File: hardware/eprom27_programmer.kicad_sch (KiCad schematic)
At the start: 37 parts, among them IC1 74595D, IC2 74595D, IC3 27512, J1 JACK-PLUG1, Q1 BC557, Q2 BC557, Q3 BC557, Q4 BC557, Q5 BC557, Q6 BC547, Q7 BC547, Q8 BC547, U1 NANO, U2 DC-DC-STEP-UP-MT3608, X1 MPT2

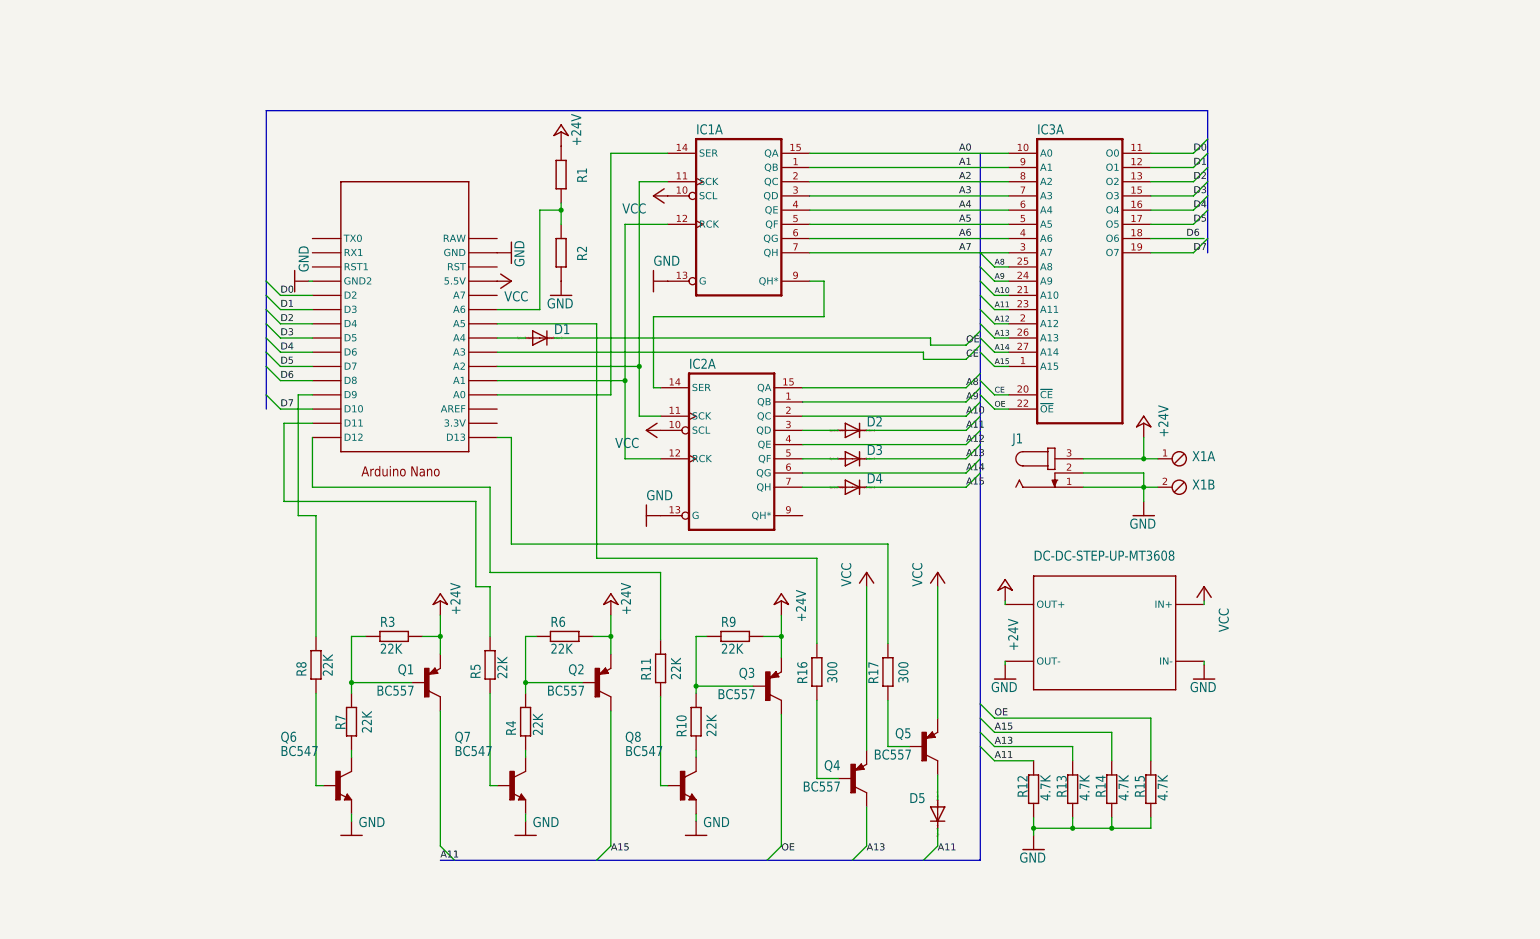
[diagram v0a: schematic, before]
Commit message: Change symbols to KiCAD Symbols Change footrpints to KiCAD footprints Redesign as all through-hole components Update gitignore
Signed-off-by: Ilias Daradimos <judgedrid@gmail.com>
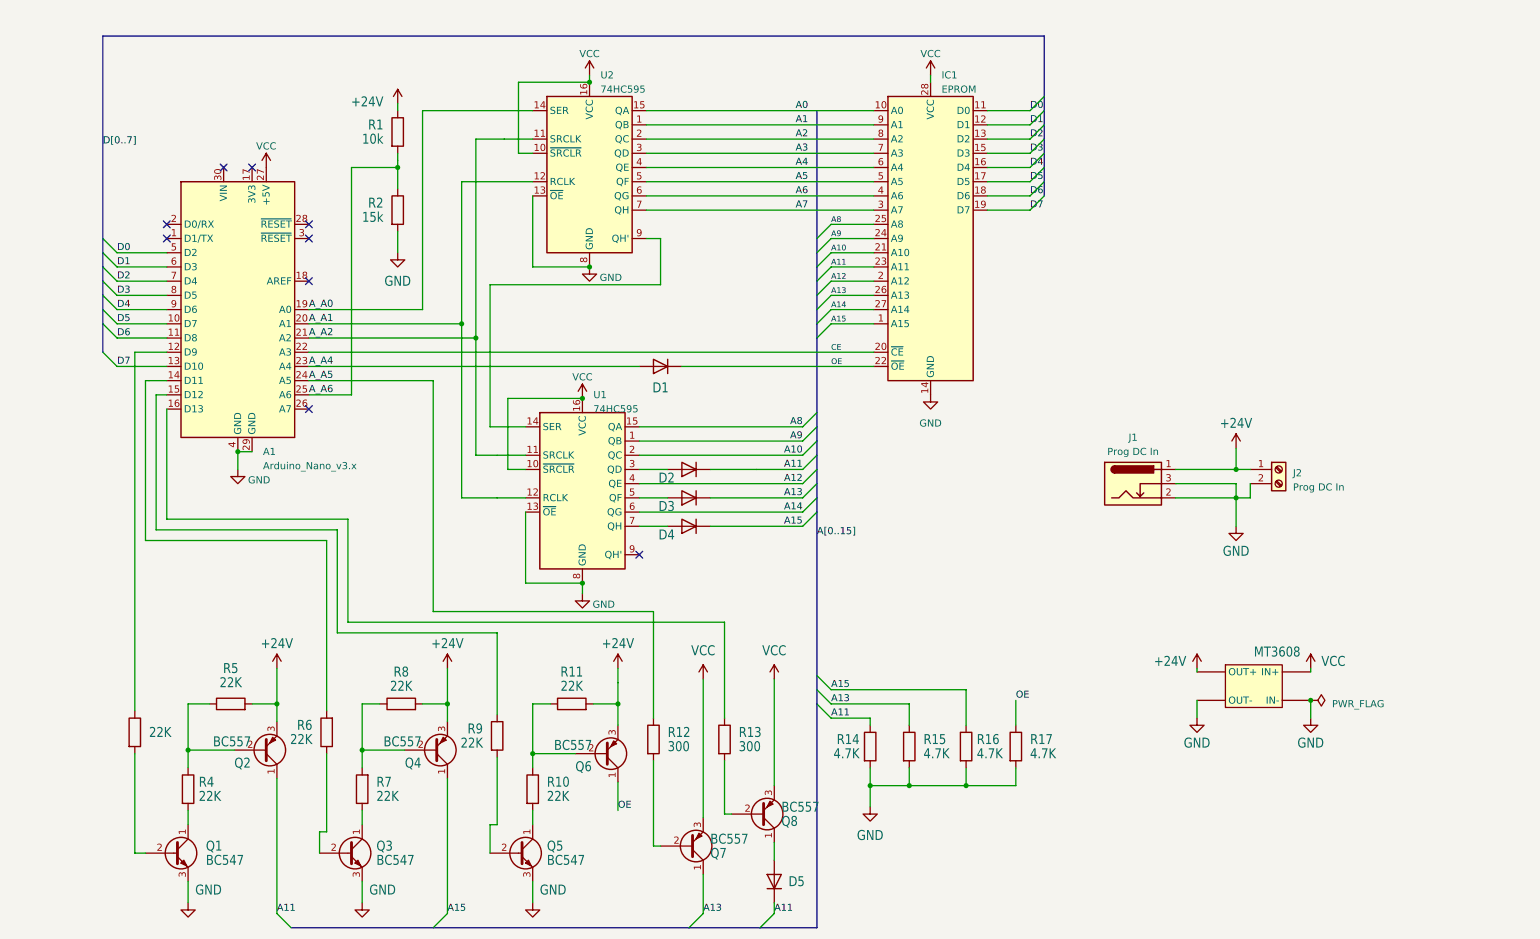
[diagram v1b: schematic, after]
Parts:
- removed IC1, IC2: 74595D, untitled:SO16, symbol untitled-eagle-import:74595D
- removed IC3: 27512, untitled:DIL28, symbol untitled-eagle-import:27512
- removed J1: JACK-PLUG1, untitled:SPC4078, symbol untitled-eagle-import:JACK-PLUG1
- removed U1: NANO, untitled:NANO, symbol untitled-eagle-import:NANO
- removed X1: MPT2, untitled:2POL254, symbol untitled-eagle-import:MPT2
- added A1: Arduino_Nano_v3.x, Module:Arduino_Nano, symbol MCU_Module:Arduino_Nano_v3.x
- added IC1: EPROM, Socket:DIP_Socket-28_W11.9_W12.7_W15.24_W17.78_W18.5_3M_228-1277-00-0602J, symbol Memory_EPROM:27512
- added J1: Prog DC In, Connector_BarrelJack:BarrelJack_Wuerth_6941xx301002, symbol Connector:Barrel_Jack_Switch
- added J2: Prog DC In, TerminalBlock_Phoenix:TerminalBlock_Phoenix_MKDS-1,5-2-5.08_1x02_P5.08mm_Horizontal, symbol Connector:Screw_Terminal_01x02
- added U1, U2: 74HC595, Package_DIP:DIP-16_W7.62mm, symbol 74xx:74HC595
- D1, D2, D3, D4, D5: footprint untitled:DO35-10 -> Diode_THT:D_DO-35_SOD27_P7.62mm_Horizontal; symbol untitled-eagle-import:1N4446 -> Diode:1N4448
- M1: renamed from U2; value DC-DC-STEP-UP-MT3608 -> MT3608; footprint untitled:DC-DC-STEP-UP-MT3608 -> eprom27:DC-DC-STEP-UP-MT3608; symbol untitled-eagle-import:DC-DC-STEP-UP-MT3608 -> eprom27_programmer:DC-DC-STEP-UP-MT3608
- Q1: renamed from Q6; footprint untitled:TO92 -> Package_TO_SOT_THT:TO-92_Inline; symbol untitled-eagle-import:BC547 -> Transistor_BJT:BC547
- Q2: renamed from Q1; footprint untitled:TO92 -> Package_TO_SOT_THT:TO-92_Inline; symbol untitled-eagle-import:BC557 -> Transistor_BJT:BC557
- Q3: renamed from Q7; footprint untitled:TO92 -> Package_TO_SOT_THT:TO-92_Inline; symbol untitled-eagle-import:BC547 -> Transistor_BJT:BC547
- Q4: renamed from Q2; footprint untitled:TO92 -> Package_TO_SOT_THT:TO-92_Inline; symbol untitled-eagle-import:BC557 -> Transistor_BJT:BC557
- Q5: renamed from Q8; footprint untitled:TO92 -> Package_TO_SOT_THT:TO-92_Inline; symbol untitled-eagle-import:BC547 -> Transistor_BJT:BC547
- Q6: renamed from Q3; footprint untitled:TO92 -> Package_TO_SOT_THT:TO-92_Inline; symbol untitled-eagle-import:BC557 -> Transistor_BJT:BC557
- Q7: renamed from Q4; footprint untitled:TO92 -> Package_TO_SOT_THT:TO-92_Inline; symbol untitled-eagle-import:BC557 -> Transistor_BJT:BC557
- Q8: renamed from Q5; footprint untitled:TO92 -> Package_TO_SOT_THT:TO-92_Inline; symbol untitled-eagle-import:BC557 -> Transistor_BJT:BC557
- R1: value R-EU_M0805 -> 10k; footprint untitled:M0805 -> Resistor_THT:R_Axial_DIN0207_L6.3mm_D2.5mm_P7.62mm_Horizontal; symbol untitled-eagle-import:R-EU_M0805 -> Device:R
- R10: footprint untitled:M0805 -> Resistor_THT:R_Axial_DIN0207_L6.3mm_D2.5mm_P7.62mm_Horizontal; symbol untitled-eagle-import:R-EU_M0805 -> Device:R
- R11: renamed from R9; footprint untitled:M0805 -> Resistor_THT:R_Axial_DIN0207_L6.3mm_D2.5mm_P7.62mm_Horizontal; symbol untitled-eagle-import:R-EU_M0805 -> Device:R
- R12: renamed from R16; footprint untitled:M0805 -> Resistor_THT:R_Axial_DIN0207_L6.3mm_D2.5mm_P7.62mm_Horizontal; symbol untitled-eagle-import:R-EU_M0805 -> Device:R
- R13: renamed from R17; footprint untitled:M0805 -> Resistor_THT:R_Axial_DIN0207_L6.3mm_D2.5mm_P7.62mm_Horizontal; symbol untitled-eagle-import:R-EU_M0805 -> Device:R
- R14: renamed from R12; footprint untitled:M0805 -> Resistor_THT:R_Axial_DIN0207_L6.3mm_D2.5mm_P7.62mm_Horizontal; symbol untitled-eagle-import:R-EU_M0805 -> Device:R
- R15: renamed from R13; footprint untitled:M0805 -> Resistor_THT:R_Axial_DIN0207_L6.3mm_D2.5mm_P7.62mm_Horizontal; symbol untitled-eagle-import:R-EU_M0805 -> Device:R
- R16: renamed from R14; footprint untitled:M0805 -> Resistor_THT:R_Axial_DIN0207_L6.3mm_D2.5mm_P7.62mm_Horizontal; symbol untitled-eagle-import:R-EU_M0805 -> Device:R
- R17: renamed from R15; footprint untitled:M0805 -> Resistor_THT:R_Axial_DIN0207_L6.3mm_D2.5mm_P7.62mm_Horizontal; symbol untitled-eagle-import:R-EU_M0805 -> Device:R
- R2: value R-EU_M0805 -> 15k; footprint untitled:M0805 -> Resistor_THT:R_Axial_DIN0207_L6.3mm_D2.5mm_P7.62mm_Horizontal; symbol untitled-eagle-import:R-EU_M0805 -> Device:R
- R3: renamed from R8; footprint untitled:M0805 -> Resistor_THT:R_Axial_DIN0207_L6.3mm_D2.5mm_P7.62mm_Horizontal; symbol untitled-eagle-import:R-EU_M0805 -> Device:R
- R4: renamed from R7; footprint untitled:M0805 -> Resistor_THT:R_Axial_DIN0207_L6.3mm_D2.5mm_P7.62mm_Horizontal; symbol untitled-eagle-import:R-EU_M0805 -> Device:R
- R5: renamed from R3; footprint untitled:M0805 -> Resistor_THT:R_Axial_DIN0207_L6.3mm_D2.5mm_P7.62mm_Horizontal; symbol untitled-eagle-import:R-EU_M0805 -> Device:R
- R6: renamed from R5; footprint untitled:M0805 -> Resistor_THT:R_Axial_DIN0207_L6.3mm_D2.5mm_P7.62mm_Horizontal; symbol untitled-eagle-import:R-EU_M0805 -> Device:R
- R7: renamed from R4; footprint untitled:M0805 -> Resistor_THT:R_Axial_DIN0207_L6.3mm_D2.5mm_P7.62mm_Horizontal; symbol untitled-eagle-import:R-EU_M0805 -> Device:R
- R8: renamed from R6; footprint untitled:M0805 -> Resistor_THT:R_Axial_DIN0207_L6.3mm_D2.5mm_P7.62mm_Horizontal; symbol untitled-eagle-import:R-EU_M0805 -> Device:R
- R9: renamed from R11; footprint untitled:M0805 -> Resistor_THT:R_Axial_DIN0207_L6.3mm_D2.5mm_P7.62mm_Horizontal; symbol untitled-eagle-import:R-EU_M0805 -> Device:R
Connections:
- net +24V: now also Q2.3 (E), Q4.3 (E), Q6.3 (E), J1.1, J2.1 (Pin_1); no longer Q2.1 (E), Q4.1 (E), Q6.1 (E)
- net A0: now also IC1.10 (A0), U2.15 (QA)
- net A1: now also IC1.9 (A1), U2.1 (QB)
- net A10: now also IC1.21 (A10), U1.2 (QC)
- net A11: now also D2.1 (K), D5.1 (K), Q2.1 (C), IC1.23 (A11); no longer D2.C
- net A12: now also IC1.2 (A12), U1.4 (QE)
- net A13: now also D3.1 (K), Q7.1 (C), IC1.26 (A13); no longer D3.C
- net A14: now also IC1.27 (A14), U1.6 (QG)
- net A15: now also D4.1 (K), Q4.1 (C), IC1.1 (A15); no longer D4.C
- net A2: now also IC1.8 (A2), U2.2 (QC)
- net A3: now also IC1.7 (A3), U2.3 (QD)
- net A4: now also IC1.6 (A4), U2.4 (QE)
- net A5: now also IC1.5 (A5), U2.5 (QF)
- net A6: now also IC1.4 (A6), U2.6 (QG)
- net A7: now also IC1.3 (A7), U2.7 (QH)
- net A8: now also IC1.25 (A8), U1.15 (QA)
- net A9: now also IC1.24 (A9), U1.1 (QB)
- net CE: now also A1.22 (A3), IC1.20 (~{CE})
- net D0: now also A1.5 (D2), IC1.11 (D0)
- net D1: now also A1.6 (D3), IC1.12 (D1)
- net D2: now also A1.7 (D4), IC1.13 (D2)
- net D3: now also A1.8 (D5), IC1.15 (D3)
- net D4: now also A1.9 (D6), IC1.16 (D4)
- net D5: now also A1.10 (D7), IC1.17 (D5)
- net D6: now also A1.11 (D8), IC1.18 (D6)
- net D7: now also A1.13 (D10), IC1.19 (D7)
- net GND: now also Q1.3 (E), Q3.3 (E), Q5.3 (E), A1.29 (GND), A1.4 (GND), IC1.14 (GND), J1.2, J1.3, J2.2 (Pin_2), U1.13 (~{OE}), U1.8 (GND), U2.13 (~{OE}), U2.8 (GND); no longer Q1.1 (E), Q3.1 (E), Q5.1 (E)
- net OE: now also D1.1 (K), Q6.1 (C), IC1.22 (~{OE}); no longer D1.C
- net VCC: now also Q7.3 (E), Q8.3 (E), A1.27 (+5V), IC1.28 (VCC), U1.10 (~{SRCLR}), U1.16 (VCC), U2.10 (~{SRCLR}), U2.16 (VCC); no longer Q7.1 (E), Q8.1 (E)
- net A_A5: now reaches R12.1
- net A_A5: now also A1.24 (A5)
- net at R7.1: now also Q3.1 (C); no longer Q3.3 (C)
- net A_A6: now reaches R1.2, R2.1
- net A_A6: now also A1.25 (A6)
- net at R6.2: now also A1.14 (D11)
- net at R9.1: now also A1.15 (D12)
- net at R13.1: now also A1.16 (D13)
- net at R3.1: now also A1.12 (D9)
- net at R10.2: now also Q5.1 (C); no longer Q5.3 (C)
- net at R4.2: now also Q1.1 (C); no longer Q1.3 (C)
- new net: D5.2 (A), Q8.1 (C)
- new net: U1.14 (SER), U2.9 (QH')
- new net: D2.2 (A), U1.3 (QD)
- new net: D3.2 (A), U1.5 (QF)
- new net: D4.2 (A), U1.7 (QH)
- new net A_A0: A1.19 (A0), U2.14 (SER)
- new net A_A1: A1.20 (A1), U1.12 (RCLK), U2.12 (RCLK)
- new net A_A2: A1.21 (A2), U1.11 (SRCLK), U2.11 (SRCLK)
- new net A_A4: A1.23 (A4), D1.2 (A)
- no-connect marks 0 -> 9
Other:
- title: (none) -> ${title}

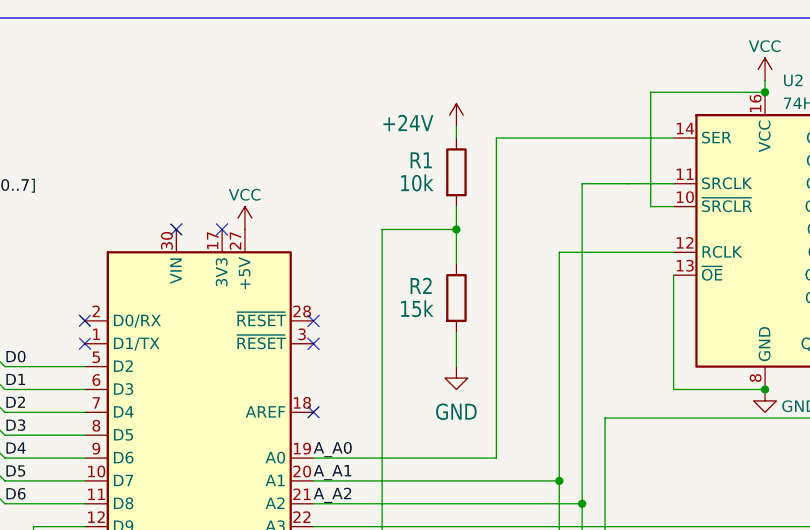
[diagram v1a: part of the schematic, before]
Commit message: Set ADC range to 30V
Signed-off-by: Ilias Daradimos <judgedrid@gmail.com>
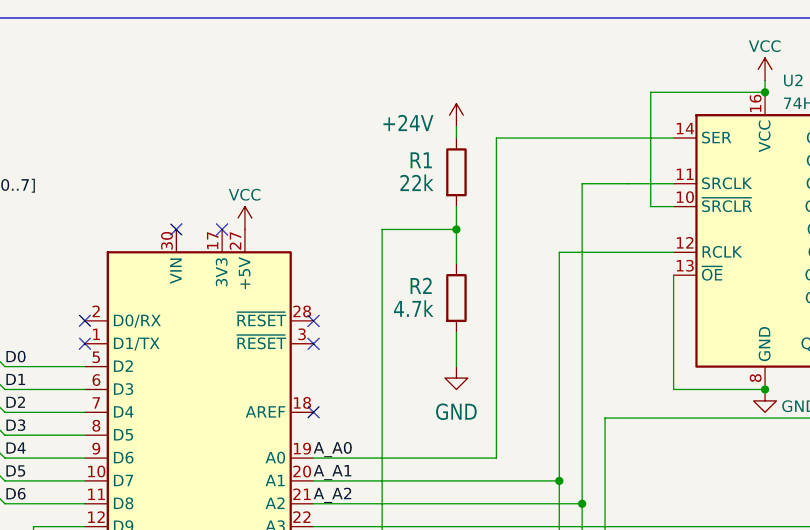
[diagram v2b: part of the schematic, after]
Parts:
- R1: value 10k -> 22k
- R2: value 15k -> 4.7k
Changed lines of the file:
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@@
       (effects (font (size 1.778 1.5113)) (justify right))
     )
-    (property "Value" "10k" (at 81.28 40.64 0)
+    (property "Value" "22k" (at 81.28 40.64 0)
       (effects (font (size 1.778 1.5113)) (justify right))
     )
@@
       (effects (font (size 1.778 1.5113)) (justify right))
     )
-    (property "Value" "15k" (at 81.28 54.61 0)
+    (property "Value" "4.7k" (at 81.28 54.61 0)
       (effects (font (size 1.778 1.5113)) (justify right))
     )

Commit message: Add EPROM ID and EEPROM Erase connection
Signed-off-by: Ilias Daradimos <judgedrid@gmail.com>
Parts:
- added D6: 1N4446, Diode_THT:D_DO-35_SOD27_P7.62mm_Horizontal, symbol Diode:1N4448
- added Q10: BC557, Package_TO_SOT_THT:TO-92_Inline, symbol Transistor_BJT:BC557
- added Q9: BC547, Package_TO_SOT_THT:TO-92_Inline, symbol Transistor_BJT:BC547
- added R18, R19, R20: 22K, Resistor_THT:R_Axial_DIN0207_L6.3mm_D2.5mm_P7.62mm_Horizontal, symbol Device:R
- R1: value 22k -> 10k
- R2: value 4.7k -> 15k
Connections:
- net +24V: now also Q10.3 (E), R20.2
- net A9: now also D6.1 (K), Q10.1 (C); no longer U1.1 (QB)
- net GND: now also Q9.3 (E)
- net at A1.26 (A7): now also R18.1
- new net: D6.2 (A), U1.1 (QB)
- new net: Q10.2 (B), R19.1, R20.1
- new net: Q9.1 (C), R19.2
- new net: Q9.2 (B), R18.2
- no-connect marks 9 -> 8
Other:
- moved on the sheet: A1, D1, D2, D3, D4, D5, IC1, J1, J2, Q1, Q2, Q3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
